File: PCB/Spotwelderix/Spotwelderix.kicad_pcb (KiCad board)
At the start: 2 copper layers, 100 x 70 mm, 58 parts, among them IC1 INA213AIDCKR, IC2 IXDD604SIA, IC3 IXDD604SIA, J1 OnOffTast, J2 probe+, J3 Conn_01x02_Male, J4 probe-, J5 TestCurr, J6 Conn_01x02_Male, P1 CONN_01X09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

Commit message: V2 tweaks and tricks
Voltmeasure enable
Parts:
- removed J5: TestCurr, Connector_PinHeader_2.54mm:PinHeader_1x02_P2.54mm_Vertical
- added C18: 470p, Capacitor_SMD:C_0805_2012Metric_Pad1.18x1.45mm_HandSolder, F.Cu at (121.0, 75.4)
- added Q11: BC817, Package_TO_SOT_SMD:SOT-23, F.Cu at (121.2, 62.5)
- added Q12: BC807, Package_TO_SOT_SMD:SOT-23, F.Cu at (118.2, 66.4)
- added R10: 470, Resistor_SMD:R_0805_2012Metric, F.Cu at (125.2, 62.5)
- added R13: 47k, Resistor_SMD:R_0805_2012Metric, F.Cu at (118.1, 69.8)
- added R14: 47k, Resistor_SMD:R_0805_2012Metric, F.Cu at (111.8, 66.4)
- added R4: 10k, Resistor_SMD:R_0805_2012Metric, F.Cu at (125.2, 66.4)
- C17: value 1µ -> 470p
- R11: value 12 -> 47k
- R12: value 12 -> 10k
- moved C17 53.3 mm to (113.6, 69.8), turned to 180 degrees
- moved R12 50.3 mm to (117.8, 62.5), turned to 90 degrees
- moved R11 41.5 mm to (122.0, 66.4), turned to 90 degrees
- moved D2 13.4 mm to (105.9, 88.2)
- moved R5 10.8 mm to (113.7, 74.2)
- moved R2 8.16 mm to (122.3, 70.0)
- moved C15 6.47 mm to (112.0, 62.5), turned to 90 degrees
- moved Q9 5.60 mm to (117.6, 75.6)
- moved R6 5.02 mm to (113.7, 76.4)
- moved R8 4.60 mm to (114.8, 62.5), turned to 90 degrees
- moved Q10 3.77 mm to (118.9, 79.3)
- moved C16 3.26 mm to (160.2, 91.2), turned to 0 degrees
- moved J1 2.97 mm to (142.8, 96.0)
- moved H6 2.09 mm to (169.4, 96.0)
- moved H5 2.01 mm to (129.2, 96.0)
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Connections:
- C17 pad 1: Net-(C17-Pad1) -> R_Schunt_Stab
- C17 pad 2: Net-(C17-Pad2) -> GND
- IC1 pad 4: Net-(C17-Pad2) -> +BATT
- IC1 pad 5: Net-(C17-Pad1) -> VCCQ
- IC1 pad 6: R_Schunt_Stab -> Net-(IC1-Pad6)
- IC2 pad 1: Net-(IC2-Pad1) -> VCC
- IC2 pad 8: Net-(IC2-Pad8) -> VCC
- IC3 pad 1: Net-(IC3-Pad1) -> VCC
- IC3 pad 8: Net-(IC3-Pad8) -> VCC
- R11 pad 1: Net-(C17-Pad2) -> VCCQ
- R11 pad 2: +BATT -> Net-(Q12-Pad1)
- R12 pad 1: Net-(C17-Pad1) -> Net-(Q12-Pad1)
- R12 pad 2: VCCQ -> Net-(Q11-Pad3)
- R7 pad 1: Net-(D2-Pad2) -> Net-(Q12-Pad2)
- R7 pad 2: V_Batt -> Net-(R14-Pad1)
- R8 pad 1: V_Batt -> Net-(R14-Pad1)
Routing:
- net R_Schunt_Stab: track 92.0 -> 18.4 mm, vias 1 -> 0
- net Net-(IC1-Pad6): track 0.00 -> 67.2 mm
- net VCCQ: track 83.0 -> 141.1 mm
- net Net-(J1-Pad1): track 38.4 -> 74.3 mm
- net Net-(D2-Pad2): track 41.6 -> 12.2 mm
- net Net-(C17-Pad1): track 22.5 -> 0.00 mm
- net GND: track 46.1 -> 64.6 mm, vias 14 -> 94
- net VCC: track 124.1 -> 138.6 mm, vias 4 -> 5
- net EnablePower: track 18.3 -> 29.9 mm, vias 0 -> 1
- net Net-(C17-Pad2): track 9.91 -> 0.00 mm
- net Net-(Q12-Pad1): track 0.00 -> 7.36 mm
- net +3V3: track 84.5 -> 91.6 mm, vias 0 -> 2
- net Net-(R14-Pad1): track 0.00 -> 5.61 mm
- net Net-(Q11-Pad1): track 0.00 -> 5.10 mm
- net V_Batt: track 20.1 -> 17.1 mm
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
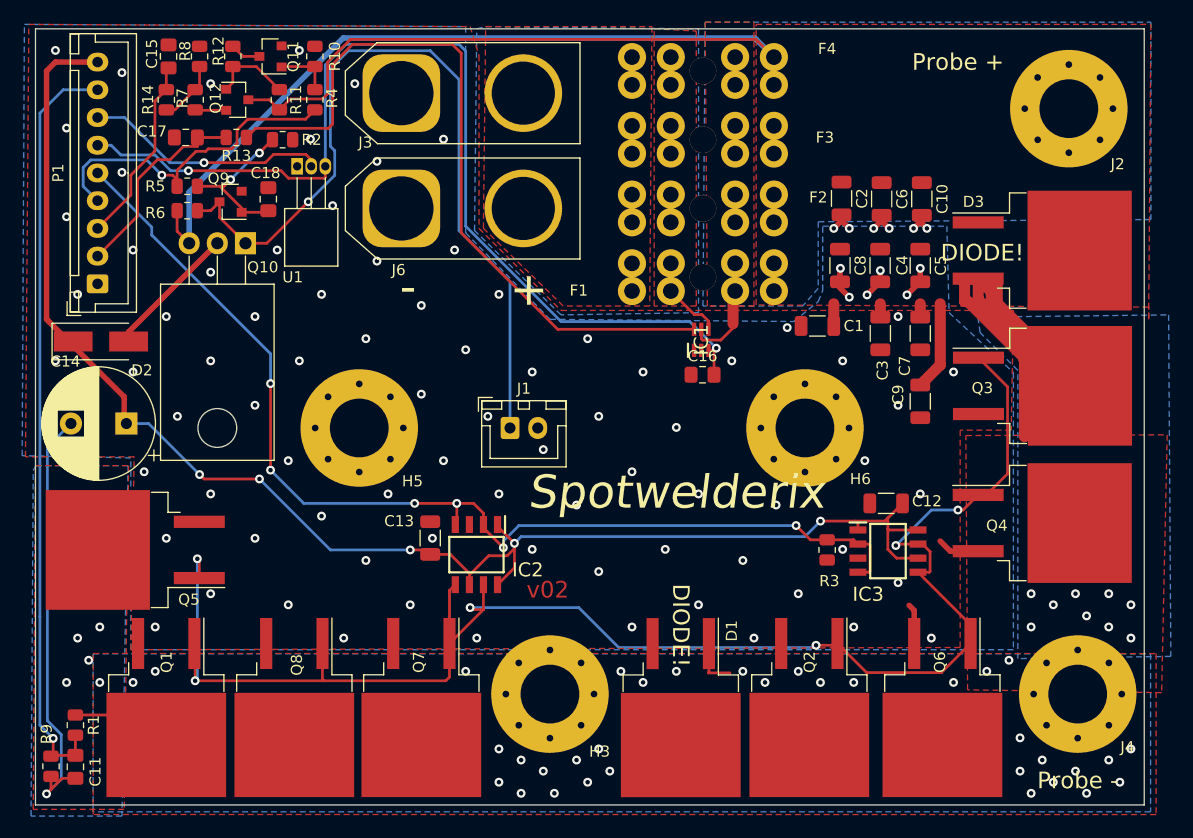
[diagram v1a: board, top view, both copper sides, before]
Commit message: connector sideflip
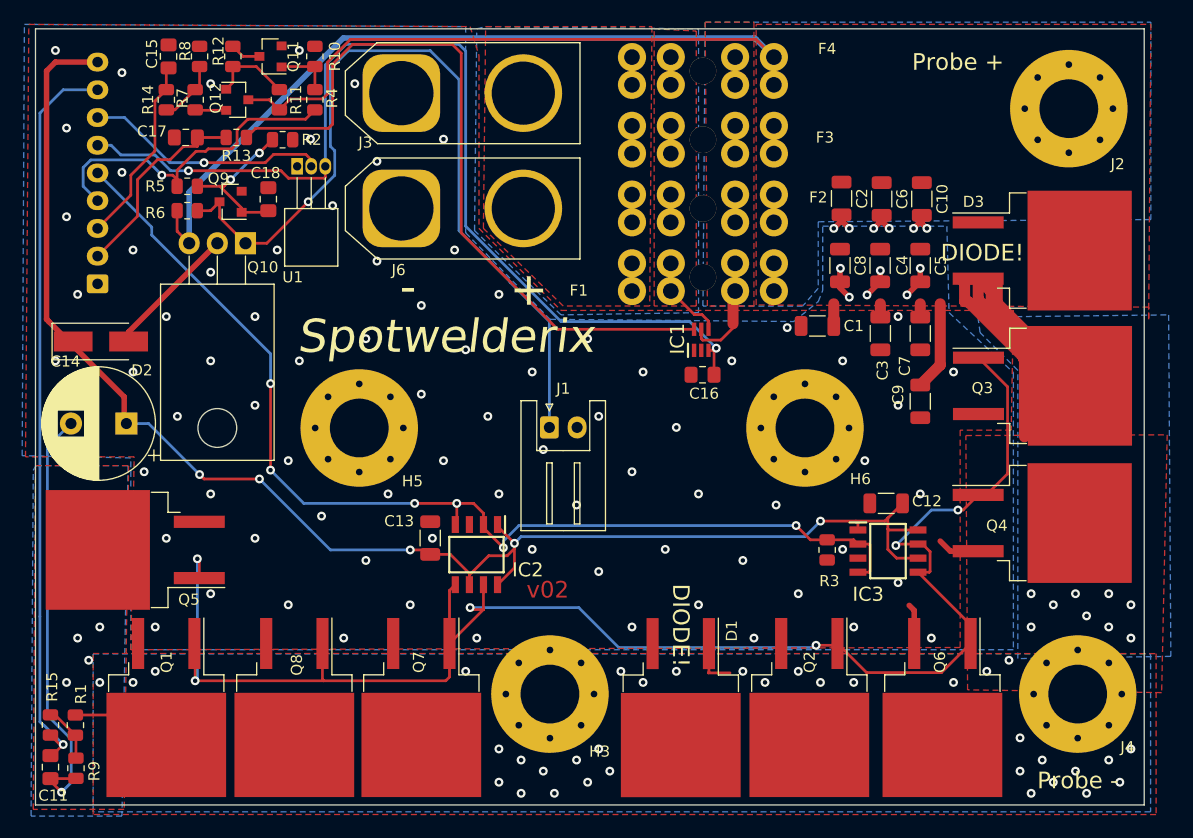
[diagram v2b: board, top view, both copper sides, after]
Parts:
- added R15: 47k, Resistor_SMD:R_0805_2012Metric, F.Cu at (101.3, 122.8)
- J1: footprint Connector_JST:JST_XH_B2B-XH-A_1x02_P2.50mm_Vertical -> Connector_JST:JST_XH_S2B-XH-A_1x02_P2.50mm_Horizontal
- P1: moved to B.Cu
- moved J1 3.55 mm to (146.3, 96.0)
- moved R9 2.26 mm to (103.7, 126.7)
- moved C11 2.25 mm to (101.3, 126.6)
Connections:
- R1 pad 2: ProbeADC -> Net-(R1-Pad2)
- R9 pad 1: ProbeADC -> Net-(R1-Pad2)
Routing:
- net Net-(R1-Pad2): track 0.00 -> 5.09 mm
- net ProbeADC: track 68.7 -> 67.0 mm
- net Net-(J1-Pad1): track 74.3 -> 75.5 mm
- net GND: track 64.6 -> 63.6 mm, vias 94 -> 93

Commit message: mount hole m4
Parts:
- H3, H5, H6: footprint MountingHole:MountingHole_5.3mm_M5_Pad_Via -> MountingHole:MountingHole_4.3mm_M4_Pad_Via
- moved C16 4.15 mm to (163.7, 89.1), turned to 180 degrees
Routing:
- net Net-(J1-Pad1): track 75.5 -> 76.6 mm
- net +3V3: track 91.6 -> 90.8 mm
- net GND: vias 93 -> 92
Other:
- board text added: "No Metal Screw!"

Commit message: clean up
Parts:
- moved C1 2.14 mm to (172.6, 87.5), turned to 270 degrees
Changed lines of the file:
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@@
     (thickness 1.6)
     (drawings 24)
-    (tracks 511)
+    (tracks 513)
     (zones 0)
     (modules 65)
@@
   )
   (setup
-    (last_trace_width 0.25)
+    (last_trace_width 1)
     (user_trace_width 0.25)
     (user_trace_width 0.5)
@@
     (tags "mounting hole 4.3mm m4")
     (attr virtual)
-    (fp_text reference H6 (at 0 -5.3) (layer F.SilkS)
+    (fp_text reference H6 (at -4.65 3.55) (layer F.SilkS)
       (effects (font (size 1 1) (thickness 0.15)))
     )
@@
     (tags "mounting hole 4.3mm m4")
     (attr virtual)
-    (fp_text reference H5 (at 0 -5.3) (layer F.SilkS)
+    (fp_text reference H5 (at -4.05 4.05) (layer F.SilkS)
       (effects (font (size 1 1) (thickness 0.15)))
     )
@@
     (tags "mounting hole 4.3mm m4")
     (attr virtual)
-    (fp_text reference H3 (at 0 -5.3) (layer F.SilkS)
+    (fp_text reference H3 (at -3.9 4.75) (layer F.SilkS)
       (effects (font (size 1 1) (thickness 0.15)))
     )
@@
   )
   (module Capacitor_SMD:C_1206_3216Metric (layer F.Cu)
-    (at 170.525 86.8 180)
+    (at 172.55 87.5 270)
     (descr "Capacitor SMD 1206 (3216 Metric), square (rectangular) end terminal, IPC_7351 nominal, (Body size source: IPC-SM-782 page 76, https://www.pcb-3d.com/wordpress/wp-content/uploads/ipc-sm-782a_amendment_1_and_2.pdf), generated with kicad-footprint-generator")
     (tags capacitor)
     (attr smd)
-    (fp_text reference C1 (at -1.525 -1.9) (layer F.SilkS)
+    (fp_text reference C1 (at 3.35 -0.05 90) (layer F.SilkS)
       (effects (font (size 1 1) (thickness 0.15)))
     )
-    (fp_text value 10µ (at 0 1.85) (layer F.Fab)
+    (fp_text value 10µ (at 0 1.85 90) (layer F.Fab)
       (effects (font (size 1 1) (thickness 0.15)))
     )
@@
     (fp_line (start 2.3 -1.15) (end 2.3 1.15) (layer F.CrtYd) (width 0.05))
     (fp_line (start 2.3 1.15) (end -2.3 1.15) (layer F.CrtYd) (width 0.05))
-    (fp_text user %R (at -0.117001 0.234999) (layer F.Fab)
+    (fp_text user %R (at -0.117001 0.234999 90) (layer F.Fab)
       (effects (font (size 0.8 0.8) (thickness 0.12)))
     )
-    (pad 2 smd roundrect (at 1.475 0 180) (size 1.15 1.8) (layers F.Cu F.Paste F.Mask) (roundrect_rratio 0.2173904347826087)
+    (pad 2 smd roundrect (at 1.475 0 270) (size 1.15 1.8) (layers F.Cu F.Paste F.Mask) (roundrect_rratio 0.2173904347826087)
       (net 1 GND))
-    (pad 1 smd roundrect (at -1.475 0 180) (size 1.15 1.8) (layers F.Cu F.Paste F.Mask) (roundrect_rratio 0.2173904347826087)
+    (pad 1 smd roundrect (at -1.475 0 270) (size 1.15 1.8) (layers F.Cu F.Paste F.Mask) (roundrect_rratio 0.2173904347826087)
       (net 8 VCCQ))
     (model ${KISYS3DMOD}/Capacitor_SMD.3dshapes/C_1206_3216Metric.wrl
@@
     (tags capacitor)
     (attr smd)
-    (fp_text reference C3 (at 3.475 0.3 90) (layer F.SilkS)
+    (fp_text reference C3 (at 3.525 0 90) (layer F.SilkS)
       (effects (font (size 1 1) (thickness 0.15)))
     )
@@
   (via (at 167.8 86.948809) (size 0.8) (drill 0.4) (layers F.Cu B.Cu) (net 1))
   (via (at 168.8 110.948809) (size 0.8) (drill 0.4) (layers F.Cu B.Cu) (net 1))
-  (via (at 172.8 89.948809) (size 0.8) (drill 0.4) (layers F.Cu B.Cu) (net 1))
+  (via (at 162.95 92.3) (size 0.8) (drill 0.4) (layers F.Cu B.Cu) (net 1))
   (via (at 172.8 106.948809) (size 0.8) (drill 0.4) (layers F.Cu B.Cu) (net 1))
   (via (at 173.8 113.948809) (size 0.8) (drill 0.4) (layers F.Cu B.Cu) (net 1))
@@
   (via (at 198.8 124.948809) (size 0.8) (drill 0.4) (layers F.Cu B.Cu) (net 7))
   (segment (start 162.9125 86.6) (end 162.9125 85.9125) (width 0.25) (layer F.Cu) (net 8))
-  (segment (start 172 86.8) (end 172 84.8) (width 1) (layer F.Cu) (net 8))
   (segment (start 176.2 86) (end 176.2 84.8) (width 1) (layer F.Cu) (net 8))
   (segment (start 179.8 86) (end 179.8 84.8) (width 1) (layer F.Cu) (net 8))
@@
   (segment (start 112.775 78.255) (end 113.86 79.34) (width 0.25) (layer F.Cu) (net 8))
   (segment (start 112.775 76.4) (end 112.775 78.255) (width 0.25) (layer F.Cu) (net 8))
+  (segment (start 172.3 85.975) (end 172.3 84.6) (width 1) (layer F.Cu) (net 8))
+  (segment (start 172.35 86.025) (end 172.3 85.975) (width 1) (layer F.Cu) (net 8))
+  (segment (start 172.55 86.025) (end 172.35 86.025) (width 1) (layer F.Cu) (net 8))
   (segment (start 108.4 87.34) (end 116.4 79.34) (width 0.5) (layer F.Cu) (net 9))
   (segment (start 108.4 88.2) (end 108.4 87.34) (width 0.5) (layer F.Cu) (net 9))
@@
     )
   )
-  (zone (net 1) (net_name GND) (layer F.Cu) (hatch edge 0.508)
-    (connect_pads (clearance 0.208))
-    (min_thickness 0.254)
-    (fill yes (arc_segments 32) (thermal_gap -0.1) (thermal_bridge_width 1))
-    (polygon
-      (pts
-        (xy 138 59.85) (xy 138 62.3) (xy 138 77.9) (xy 145.35 85.45) (xy 188.2 85.4)
-        (xy 188 96.2) (xy 183.4 96.2) (xy 183.4 115.8) (xy 108.6 116) (xy 108.9 98.6)
-        (xy 99.1 98.6) (xy 99.4 59.6)
-      )
-    )
-  )
   (zone (net 1) (net_name GND) (layer B.Cu) (hatch edge 0.508)
     (connect_pads (clearance 0.208))
@@
     (polygon
       (pts
-        (xy 155.4 85) (xy 145.8 84.95) (xy 139.3 78.2) (xy 139.2 59.9) (xy 155.6 59.8)
+        (xy 155.35 85.4) (xy 146.65 85.3) (xy 139.3 78.2) (xy 139.2 59.9) (xy 155.6 59.8)
       )
     )
@@
     (polygon
       (pts
-        (xy 159.6 85) (xy 155.8 85) (xy 155.8 60) (xy 159.6 60.2)
+        (xy 159.6 85.3) (xy 155.8 85.3) (xy 155.8 60) (xy 159.6 60.2)
       )
     )
@@
     )
   )
+  (zone (net 8) (net_name VCCQ) (layer B.Cu) (hatch edge 0.508)
+    (connect_pads (clearance 0.208))
+    (min_thickness 0.254)
+    (fill yes (arc_segments 32) (thermal_gap -0.1) (thermal_bridge_width 1))
+    (polygon
+      (pts
+        (xy 200.6 77.2) (xy 170.6 77.4) (xy 170.6 83.4) (xy 169.2 85) (xy 160.2 85)
+        (xy 160.4 59.4) (xy 200.6 59.4)
+      )
+    )
+  )
   (zone (net 8) (net_name VCCQ) (layer F.Cu) (hatch edge 0.508)
     (connect_pads (clearance 0.208))
@@
     (polygon
       (pts
-        (xy 200.4 86.2) (xy 200.4 85.1) (xy 165 84.9) (xy 165 59.6) (xy 200.6 59.6)
+        (xy 164.8 85.25) (xy 160.6 85.25) (xy 160.35 61.25) (xy 164.75 61.25)
       )
     )
   )
-  (zone (net 8) (net_name VCCQ) (layer B.Cu) (hatch edge 0.508)
+  (zone (net 7) (net_name Probe-) (layer B.Cu) (hatch edge 0.508)
     (connect_pads (clearance 0.208))
     (min_thickness 0.254)
@@
     (polygon
       (pts
-        (xy 200.6 77.2) (xy 170.6 77.4) (xy 170.6 83.4) (xy 169.2 85) (xy 160.2 85)
-        (xy 160.4 59.4) (xy 200.6 59.4)
+        (xy 202.4 116.6) (xy 188.6 116.8) (xy 188.6 90.8) (xy 185.2 87.4) (xy 185 86)
+        (xy 202.2 85.8)
       )
     )
   )
-  (zone (net 8) (net_name VCCQ) (layer F.Cu) (hatch edge 0.508)
+  (zone (net 7) (net_name Probe-) (layer F.Cu) (hatch edge 0.508)
+    (connect_pads (clearance 0.208))
+    (min_thickness 0.254)
+    (fill yes (arc_segments 32) (thermal_gap -1) (thermal_bridge_width 0.508))
+    (polygon
+      (pts
+        (xy 188.75 81.25) (xy 188.75 86.25) (xy 190.85 86.225) (xy 198.95 86.175) (xy 199 91.6)
+        (xy 189.45 91.45) (xy 186.35 88.5) (xy 182.6 85.05) (xy 182.55 85.35) (xy 182.6 81.35)
+      )
+    )
+  )
+  (zone (net 1) (net_name GND) (layer F.Cu) (hatch edge 0.508)
     (connect_pads (clearance 0.208))
     (min_thickness 0.254)
@@
     (polygon
       (pts
-        (xy 164.8 85) (xy 160.6 85) (xy 160.35 61.25) (xy 164.75 61.25)
+        (xy 138 59.85) (xy 138 77.9) (xy 146.1 86.05) (xy 173.95 86.05) (xy 182.05 86)
+        (xy 188.096374 90.995783) (xy 188 96.2) (xy 183.4 96.2) (xy 183.4 115.8) (xy 108.6 116)
+        (xy 108.9 98.6) (xy 99.1 98.6) (xy 99.4 59.6)
       )
     )
   )
-  (zone (net 7) (net_name Probe-) (layer B.Cu) (hatch edge 0.508)
+  (zone (net 8) (net_name VCCQ) (layer F.Cu) (hatch edge 0.508)
     (connect_pads (clearance 0.208))
     (min_thickness 0.254)
@@
     (polygon
       (pts
-        (xy 202.4 116.6) (xy 188.6 116.8) (xy 188.6 90.8) (xy 185.2 87.4) (xy 185 86)
-        (xy 202.2 85.8)
+        (xy 200.4 86.2) (xy 200.4 85.1) (xy 189.143674 85.036405) (xy 189.1 80.8) (xy 182.05 81)
+        (xy 182.05 85.45) (xy 165.25 85.6) (xy 165 59.6) (xy 200.6 59.6)
       )
     )
